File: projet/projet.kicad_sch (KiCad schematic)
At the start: 14 parts, among them J301 EMB_P3.81_1x02_VERTICAL, J302 EMB_P3.81_1x04_VERTICAL, U1 RASPBERRY_PI_PICO

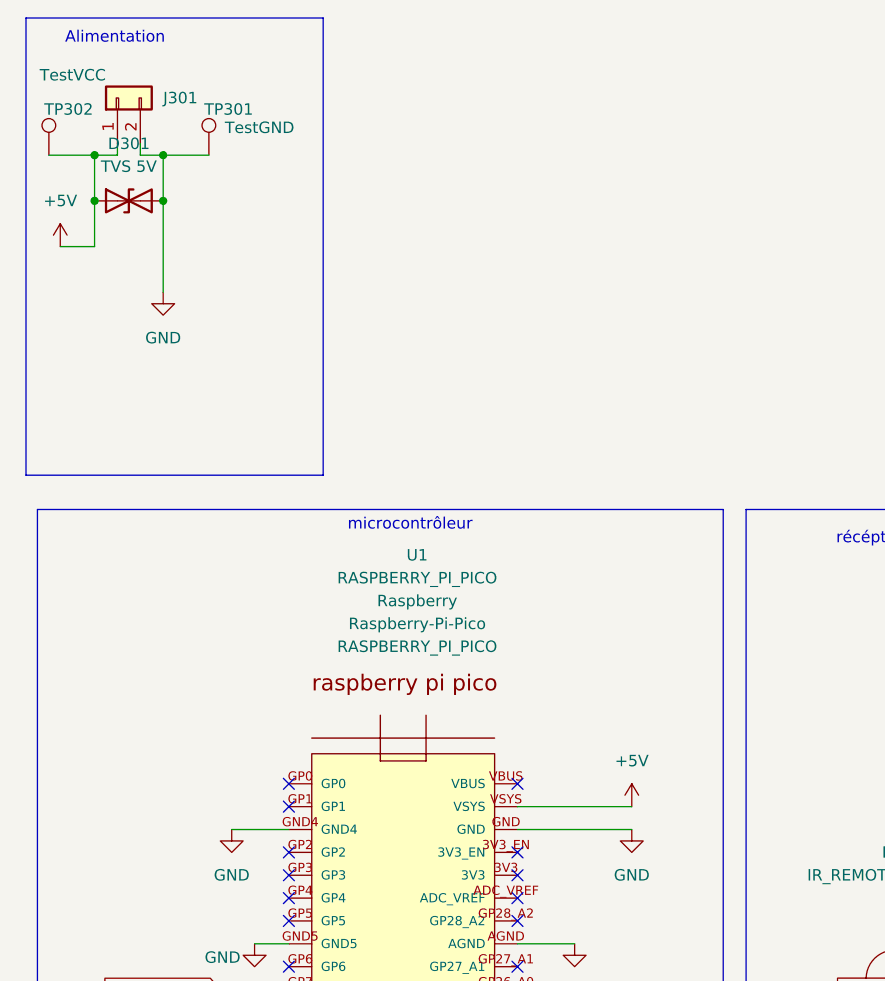
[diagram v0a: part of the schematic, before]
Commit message: ajout du mos pour gérer la double alimentation
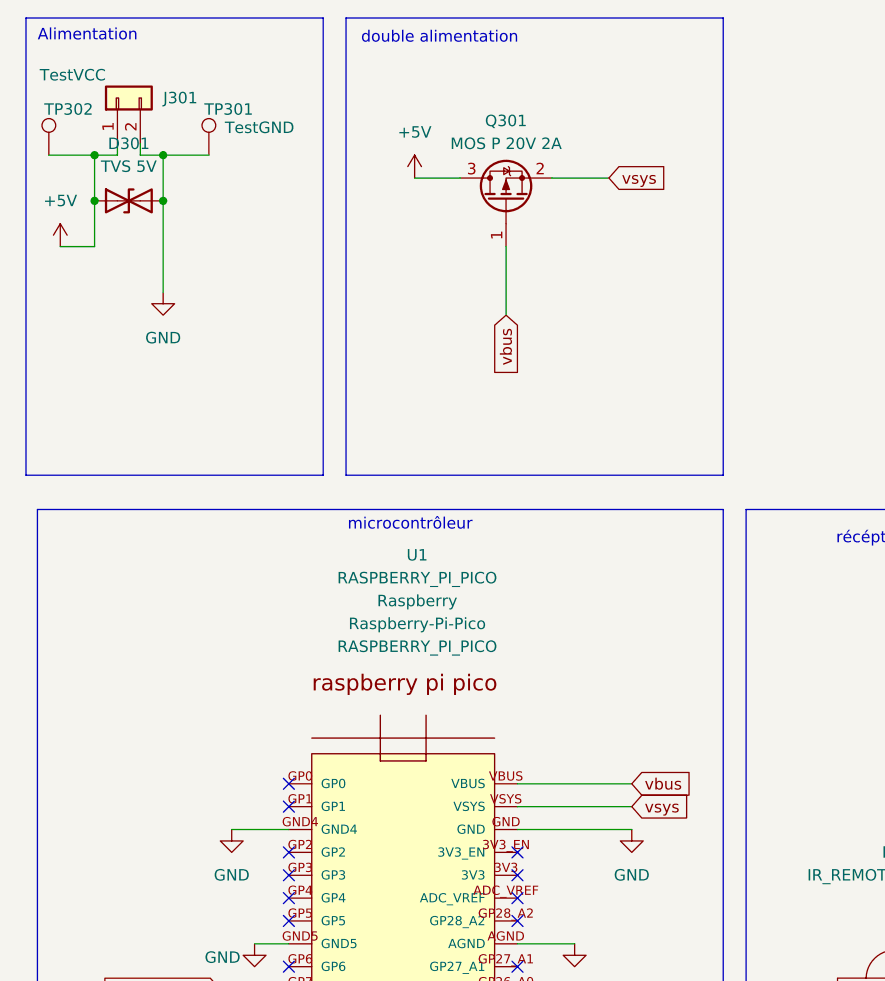
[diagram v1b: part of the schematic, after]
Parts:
- added Q301: MOS P 20V 2A, codium_Basics:SOT23, symbol codium_Transistors:Q_MOS-P_20V_2A
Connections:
- net +5V: now also Q301.3 (D); no longer U1.VSYS
- net vbus: now reaches U1.VBUS
- net vbus: now also Q301.1 (G)
- new net vsys: Q301.2 (S), U1.VSYS
- no-connect marks 30 -> 29
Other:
- note added: "double alimentation"

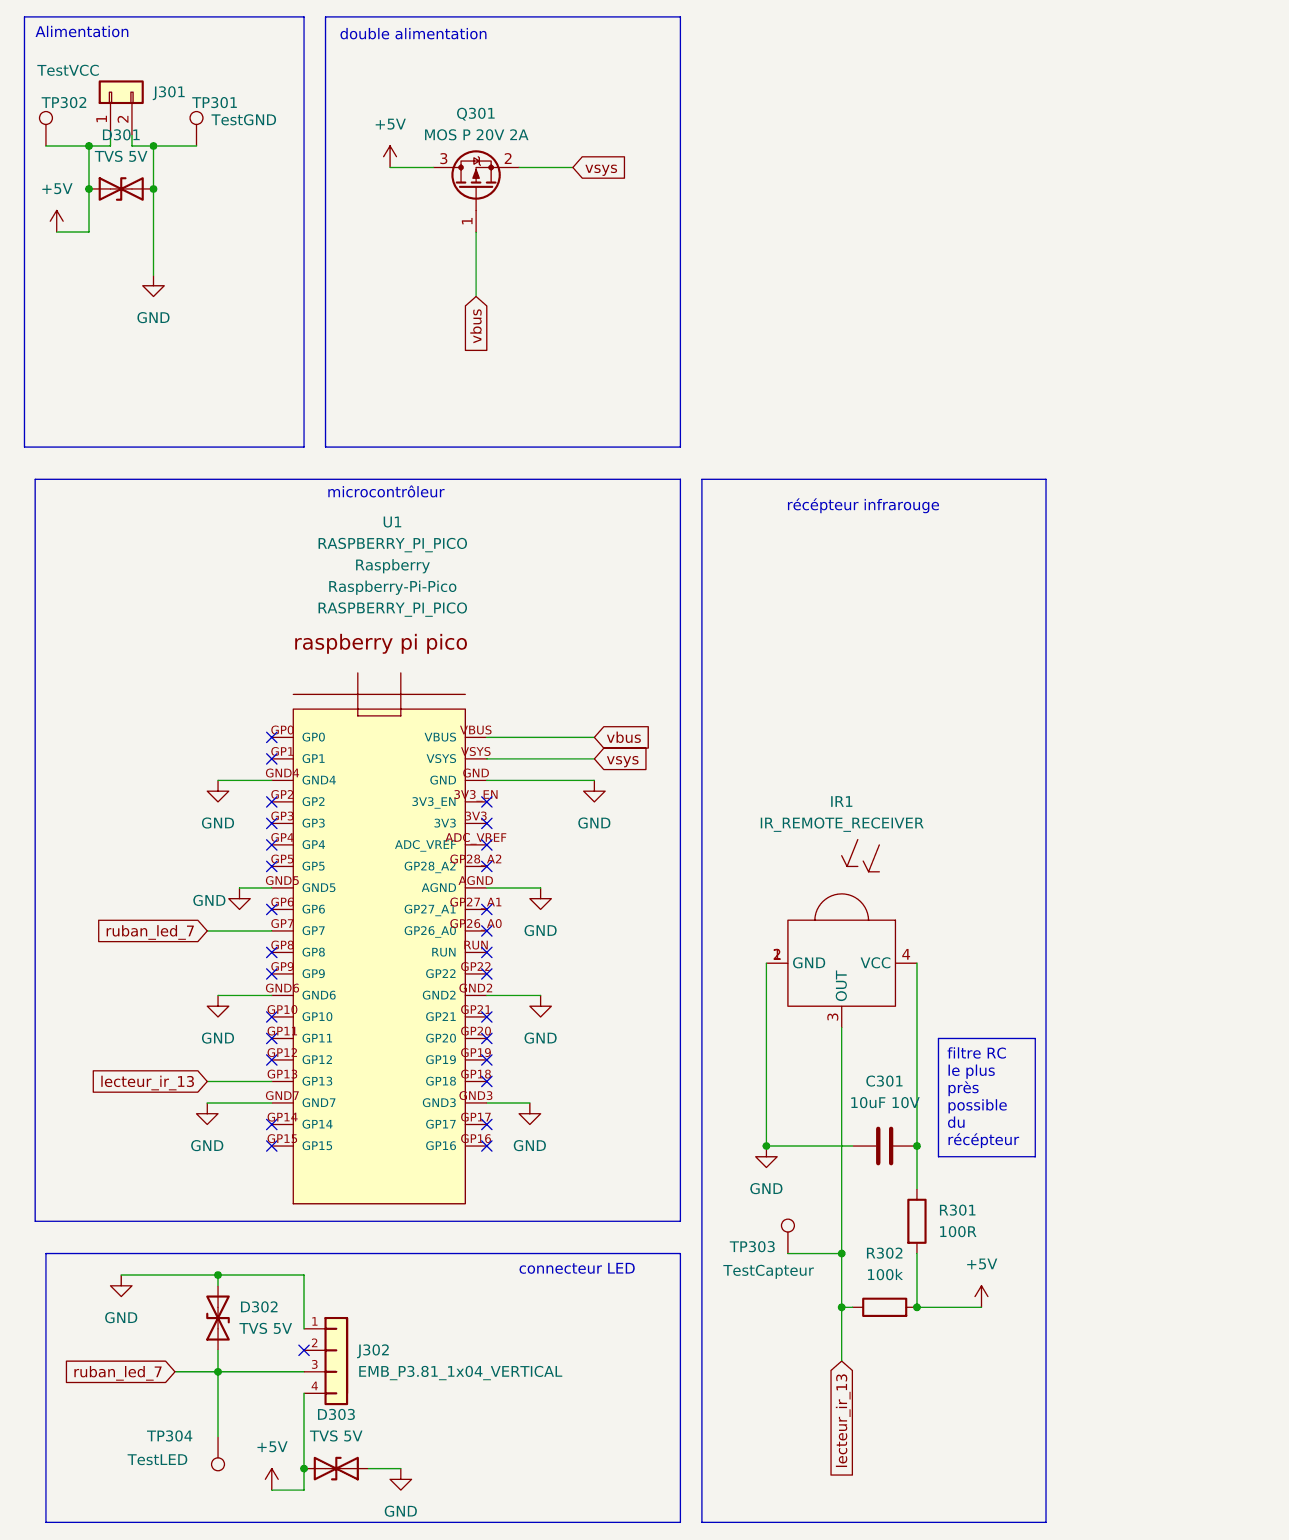
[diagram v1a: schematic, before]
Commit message: chagement du modèle de raspberry pico pour résoudre des conflits avec l'empreinte
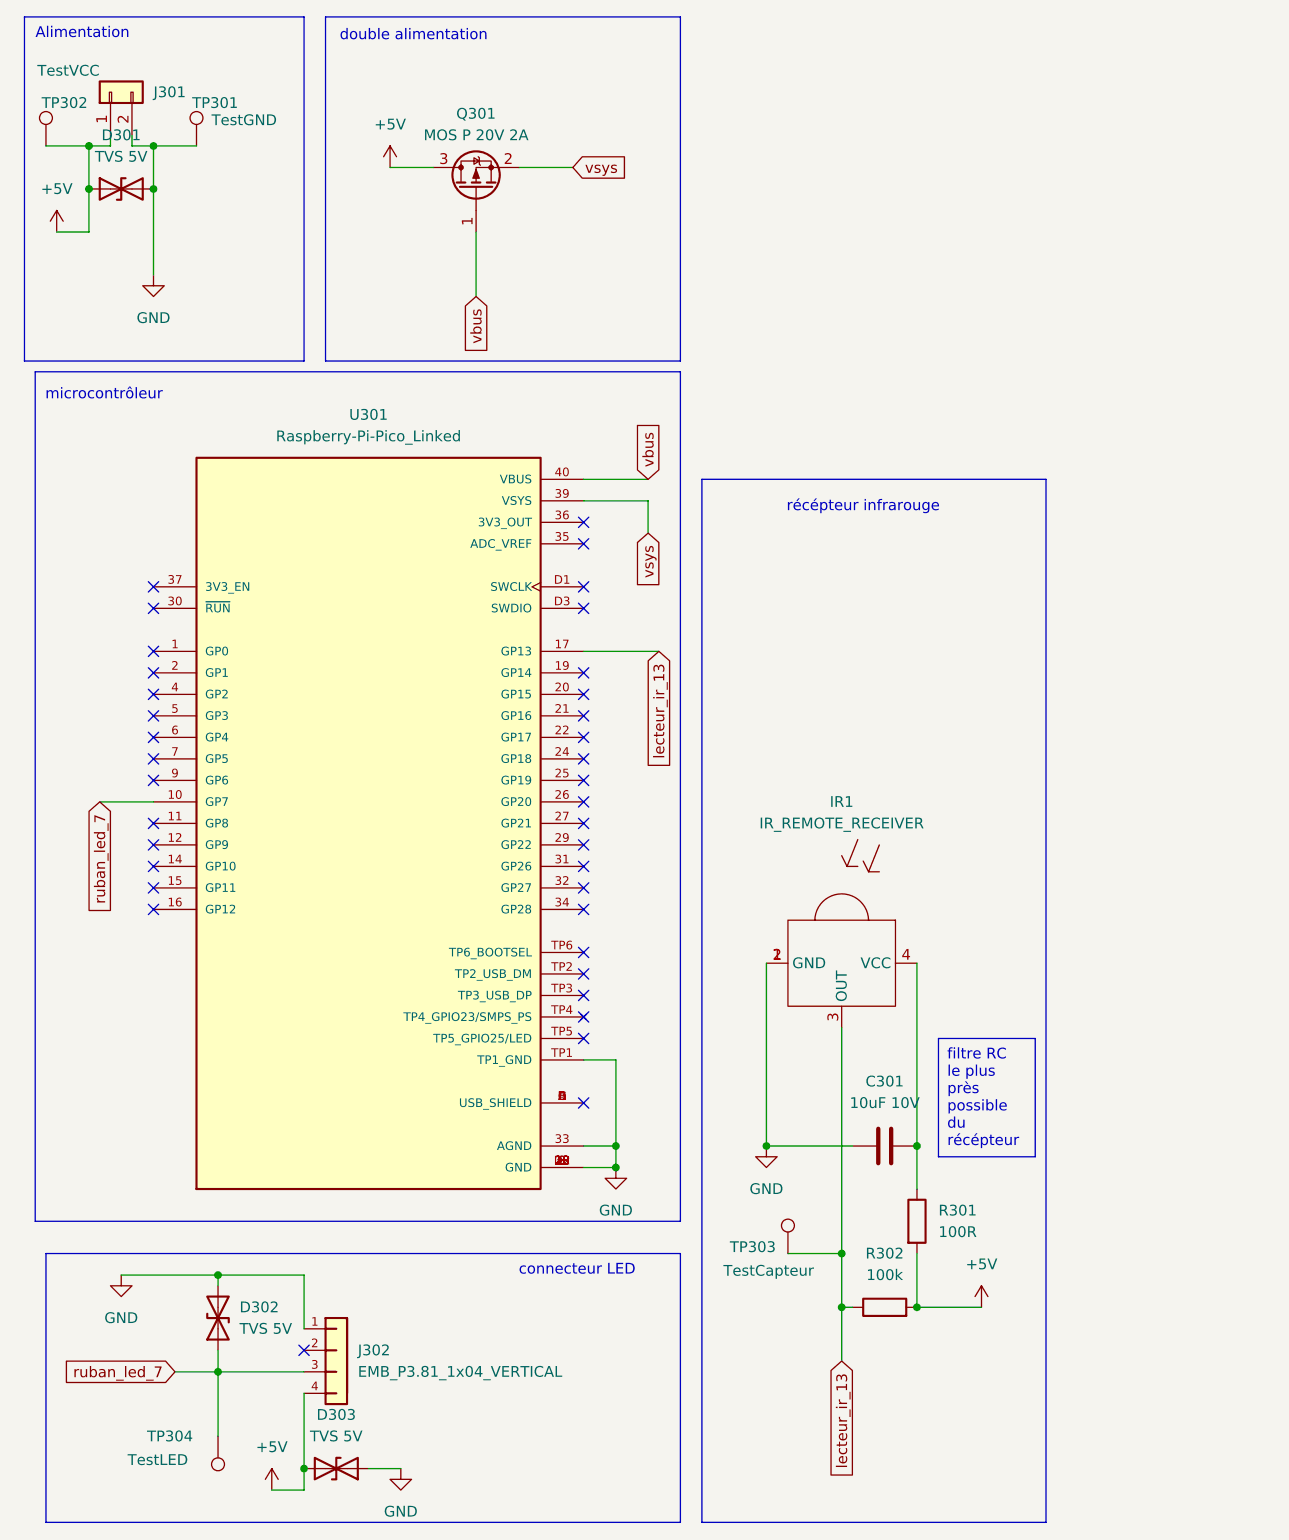
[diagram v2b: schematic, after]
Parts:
- removed U1: RASPBERRY_PI_PICO, codium_Modules:Raspberry-Pi-Pico, symbol codium_Modules:RASPBERRY_PI_PICO
- added U301: Raspberry-Pi-Pico_Linked, codium_Modules:Raspberry-Pi-Pico, symbol codium_Modules:Raspberry-Pi-Pico_Linked
- TP304: footprint (none) -> codium_Pads:TestPoint_Pad_D2.0mm
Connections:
- net GND: now also U301.13 (GND), U301.18 (GND), U301.23 (GND), U301.28 (GND), U301.3 (GND), U301.33 (AGND), U301.38 (GND), U301.8 (GND), U301.D2 (GND), U301.TP1 (TP1_GND)
- net lecteur_ir_13: now also U301.17 (GP13)
- net ruban_led_7: now also U301.10 (GP7)
- net vbus: now also U301.40 (VBUS)
- net vsys: now also U301.39 (VSYS)
- new net: U301.A (USB_SHIELD), U301.B (USB_SHIELD), U301.C (USB_SHIELD), U301.D (USB_SHIELD)
- no-connect marks 29 -> 37

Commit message: début Routage
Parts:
- TP301, TP302, TP303: footprint (none) -> codium_Pads:TestPoint_Pad_D2.0mm
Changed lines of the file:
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@@
 			)
 		)
-		(property "Footprint" ""
+		(property "Footprint" "codium_Pads:TestPoint_Pad_D2.0mm"
 			(at 109.22 160.02 0)
 			(effects
@@
 			)
 		)
-		(property "Footprint" ""
+		(property "Footprint" "codium_Pads:TestPoint_Pad_D2.0mm"
 			(at 21.59 29.21 0)
 			(effects
@@
 			)
 		)
-		(property "Footprint" ""
+		(property "Footprint" "codium_Pads:TestPoint_Pad_D2.0mm"
 			(at 39.37 29.21 0)
 			(effects

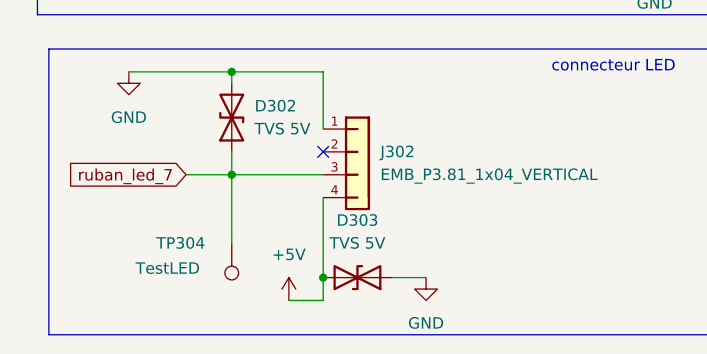
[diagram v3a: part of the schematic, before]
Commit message: ajout des capa de découplage
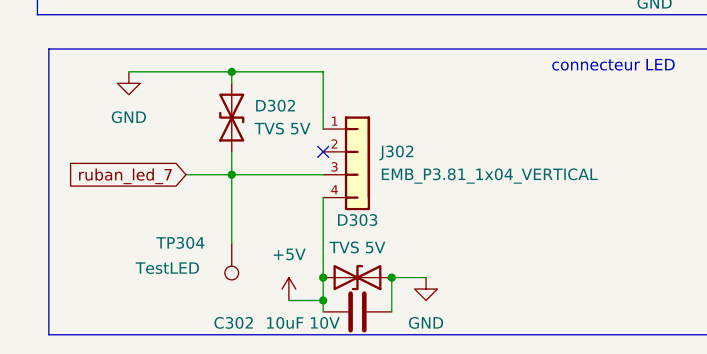
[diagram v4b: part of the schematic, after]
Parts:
- added C302: 10uF 10V, codium_Basics:C0603, symbol codium_Capacitors:C_0603_10uF_10V
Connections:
- net +5V: now also C302.1
- net GND: now also C302.2
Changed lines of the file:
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@@
+	)
+	(junction
+		(at 46.99 187.96)
+		(diameter 0)
+		(color 0 0 0 0)
 	)
 	(junction
@@
 	)
 	(junction
+		(at 54.61 185.42)
+		(diameter 0)
+		(color 0 0 0 0)
+	)
+	(junction
 		(at 101.6 147.32)
 		(diameter 0)
@@
 	(wire
 		(pts
+			(xy 54.61 185.42) (xy 54.61 189.23)
+		)
+		(stroke
+			(width 0)
+			(type default)
+		)
+	)
+	(wire
+		(pts
 			(xy 29.21 29.21) (xy 29.21 34.29)
 		)
@@
 		(pts
 			(xy 80.01 137.16) (xy 83.82 137.16)
+		)
+		(stroke
+			(width 0)
+			(type default)
+		)
+	)
+	(wire
+		(pts
+			(xy 46.99 187.96) (xy 46.99 189.23)
 		)
 		(stroke
@@
 	)
 	(symbol
+		(lib_id "codium_Capacitors:C_0603_10uF_10V")
+		(at 50.8 189.23 90)
+		(unit 1)
+		(exclude_from_sim no)
+		(in_bom yes)
+		(on_board yes)
+		(dnp no)
+		(property "Reference" "C302"
+			(at 37.084 190.5 90)
+			(effects
+				(font
+					(size 1.27 1.27)
+				)
+			)
+		)
+		(property "Value" "10uF 10V"
+			(at 44.704 190.5 90)
+			(effects
+				(font
+					(size 1.27 1.27)
+				)
+			)
+		)
+		(property "Footprint" "codium_Basics:C0603"
+			(at 54.61 188.2648 0)
+			(effects
+				(font
+					(size 1.27 1.27)
+				)
+				(hide yes)
+			)
+		)
+		(property "Datasheet" "${CODIUM_DOC_DIR}\\Capacitors\\Samsung MLCC All.pdf"
+			(at 50.8 189.23 0)
+			(effects
+				(font
+					(size 1.27 1.27)
+				)
+				(hide yes)
+			)
+		)
+		(property "Description" "MLCC X5R ±20% [RUNNER]"
+			(at 50.8 189.23 0)
+			(effects
+				(font
+					(size 1.27 1.27)
+				)
+				(hide yes)
+			)
+		)
+		(property "MAN" "Samsung"
+			(at 58.42 189.23 0)
+			(effects
+				(font
+					(size 1.27 1.27)
+				)
+				(hide yes)
+			)
+		)
+		(property "MPN" "CL10A106MP8NNNC"
+			(at 56.515 189.23 0)
+			(effects
+				(font
+					(size 1.27 1.27)
+				)
+				(hide yes)
+			)
+		)
+		(property "IPN" "C_0603_10uF_10V"
+			(at 48.26 194.945 0)
+			(effects
+				(font
+					(size 1.27 1.27)
+				)
+				(hide yes)
+			)
+		)
+		(pin "1"
+		)
+		(pin "2"
+		)
+		(instances
+			(project "projet"
+				(path "/a8729fd7-f378-4132-940e-1f2a87480560"
+					(reference "C302")
+					(unit 1)
+				)
+			)
+		)
+	)
+	(symbol
 		(lib_id "codium_Power:GND")
 		(at 29.21 44.45 0)
@@
 		(on_board yes)
 		(dnp no)
-		(fields_autoplaced yes)
 		(property "Reference" "D303"
 			(at 50.8 179.07 0)
@@
 		)
 		(property "Value" "TVS 5V"
-			(at 50.8 181.61 0)
-			(effects
-				(font
+			(at 50.8 182.118 0)
+			(effects
+				(font

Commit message: démarrage routage et installations des ports
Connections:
- net GND: now also U301.A (USB_SHIELD), U301.B (USB_SHIELD), U301.C (USB_SHIELD), U301.D (USB_SHIELD)
- no-connect marks 37 -> 35
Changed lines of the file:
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@@
+	)
+	(junction
+		(at 83.82 142.24)
+		(diameter 0)
+		(color 0 0 0 0)
 	)
 	(junction
@@
 	)
 	(no_connect
-		(at 80.01 132.08)
-	)
-	(no_connect
-		(at 80.01 142.24)
-	)
-	(no_connect
 		(at 80.01 119.38)
 	)
@@
 	(wire
 		(pts
+			(xy 80.01 142.24) (xy 83.82 142.24)
+		)
+		(stroke
+			(width 0)
+			(type default)
+		)
+	)
+	(wire
+		(pts
 			(xy 110.49 166.37) (xy 111.76 166.37)
 		)
@@
 	(wire
 		(pts
-			(xy 83.82 137.16) (xy 83.82 147.32)
+			(xy 83.82 137.16) (xy 83.82 142.24)
 		)
 		(stroke
@@
 		)
 		(stroke
+			(width 0)
+			(type default)
+		)
+	)
+	(wire
+		(pts
+			(xy 83.82 142.24) (xy 83.82 147.32)
+		)
+		(stroke

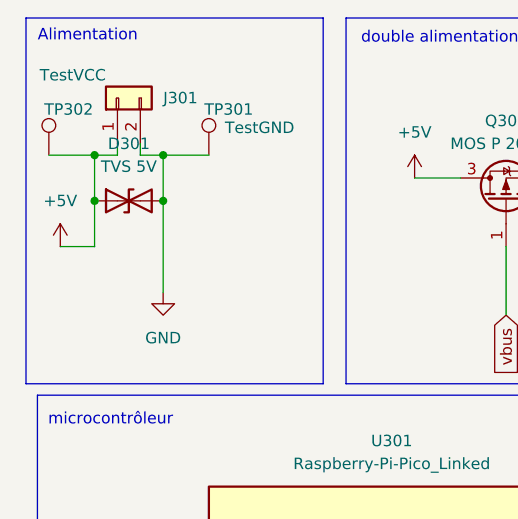
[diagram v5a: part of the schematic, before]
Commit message: ajout d'un fusible en entrée
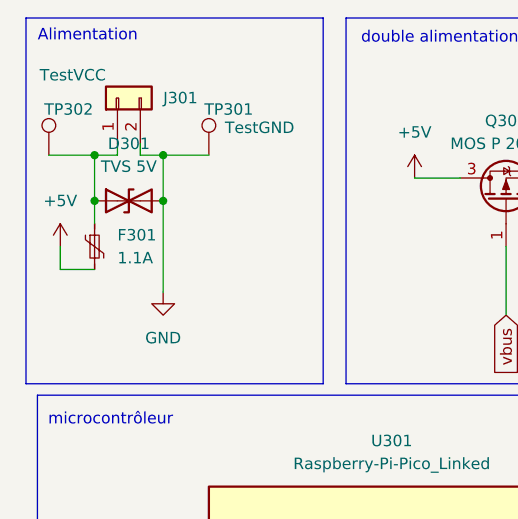
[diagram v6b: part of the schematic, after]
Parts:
- added F301: 1.1A, codium_Basics:R1812L, symbol codium_Misc:Polyswitch_1812_1.1A_24V
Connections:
- net +5V: now also F301.2; no longer D301.1 (A1), J301.1 (Pin_1), TP302.1
- new net: D301.1 (A1), F301.1, J301.1 (Pin_1), TP302.1
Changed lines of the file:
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@@
+	)
+	(junction
+		(at 21.59 34.29)
+		(diameter 0)
+		(color 0 0 0 0)
 	)
 	(junction
@@
 	)
 	(junction
-		(at 21.59 34.29)
-		(diameter 0)
-		(color 0 0 0 0)
-	)
-	(junction
 		(at 36.83 173.99)
 		(diameter 0)
@@
 	(wire
 		(pts
+			(xy 17.78 39.37) (xy 17.78 41.91)
+		)
+		(stroke
+			(width 0)
+			(type default)
+		)
+	)
+	(wire
+		(pts
 			(xy 110.49 166.37) (xy 111.76 166.37)
 		)
@@
 	(wire
 		(pts
-			(xy 17.78 39.37) (xy 21.59 39.37)
-		)
-		(stroke
-			(width 0)
-			(type default)
-		)
-	)
-	(wire
-		(pts
 			(xy 26.67 27.94) (xy 26.67 29.21)
 		)
@@
 	(wire
 		(pts
+			(xy 21.59 41.91) (xy 17.78 41.91)
+		)
+		(stroke
+			(width 0)
+			(type default)
+		)
+	)
+	(wire
+		(pts
 			(xy 80.01 149.86) (xy 83.82 149.86)
 		)
@@
 	(wire
 		(pts
+			(xy 21.59 34.29) (xy 21.59 36.83)
+		)
+		(stroke
+			(width 0)
+			(type default)
+		)
+	)
+	(wire
+		(pts
 			(xy 36.83 181.61) (xy 36.83 173.99)
 		)
@@
 		(pts
 			(xy 36.83 162.56) (xy 36.83 163.83)
-		)
-		(stroke
-			(width 0)
-			(type default)
-		)
-	)
-	(wire
-		(pts
-			(xy 21.59 39.37) (xy 21.59 34.29)
 		)
 		(stroke
@@
 					(unit 1)
 				)
+			)
+		)
+	)
+	(symbol
+		(lib_id "codium_Misc:Polyswitch_1812_1.1A_24V")
+		(at 21.59 39.37 0)
+		(unit 1)
+		(exclude_from_sim no)
+		(in_bom yes)
+		(on_board yes)
+		(dnp no)
+		(fields_autoplaced yes)
+		(property "Reference" "F301"
+			(at 24.13 38.0999 0)
+			(effects
+				(font
+					(size 1.27 1.27)
+				)
+				(justify left)
+			)
+		)
+		(property "Value" "1.1A"
+			(at 24.13 40.6399 0)
+			(effects
+				(font
+					(size 1.27 1.27)
+				)
+				(justify left)
+			)
+		)
+		(property "Footprint" "codium_Basics:R1812L"
+			(at 22.86 44.45 0)
+			(effects
+				(font
+					(size 1.27 1.27)
+				)
+				(justify left)
+				(hide yes)
+			)
+		)
+		(property "Datasheet" "${CODIUM_DOC_DIR}\\Misc\\2304140030_Littelfuse-1812L110-24DR_C207066.pdf"
+			(at 21.59 39.37 0)
+			(effects
+				(font
+					(size 1.27 1.27)
+				)
+				(hide yes)
+			)
+		)
+		(property "Description" "Polyswitch 1812 1.1A 24V"
+			(at 21.59 39.37 0)
+			(effects
+				(font
+					(size 1.27 1.27)
+				)
+				(hide yes)
+			)
+		)
+		(property "MAN" "Littlefuse"
+			(at 21.59 39.37 0)
+			(effects
+				(font
+					(size 1.27 1.27)
+				)
+				(hide yes)
+			)
+		)
+		(property "MPN" "1812L110/24DR "
+			(at 21.59 39.37 0)
+			(effects
+				(font
+					(size 1.27 1.27)
+				)
+				(hide yes)
+			)
+		)
+		(property "IPN" "Polyswitch_1.1A_24V"
+			(at 21.59 39.37 0)
+			(effects
+				(font
+					(size 1.27 1.27)
+				)
+				(hide yes)
+			)
+		)
+		(pin "1"
+		)
+		(pin "2"
+		)
+		(instances
+			(project ""
+				(path "/a8729fd7-f378-4132-940e-1f2a87480560"
+					(reference "F301")
+					(unit 1)
+				)
